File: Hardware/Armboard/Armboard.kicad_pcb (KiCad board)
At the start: 2 copper layers, 124.8 x 100.4 mm, 111 parts, among them J1 Test_Point, SW1 SW_Push, SW2 SW_Push, SW3 SW_Push, SW4 SW_Push, SW5 SW_Push, SW6 SW_Push, U1 LM2576D2TR4, U2 TM4C129E_Launchpad

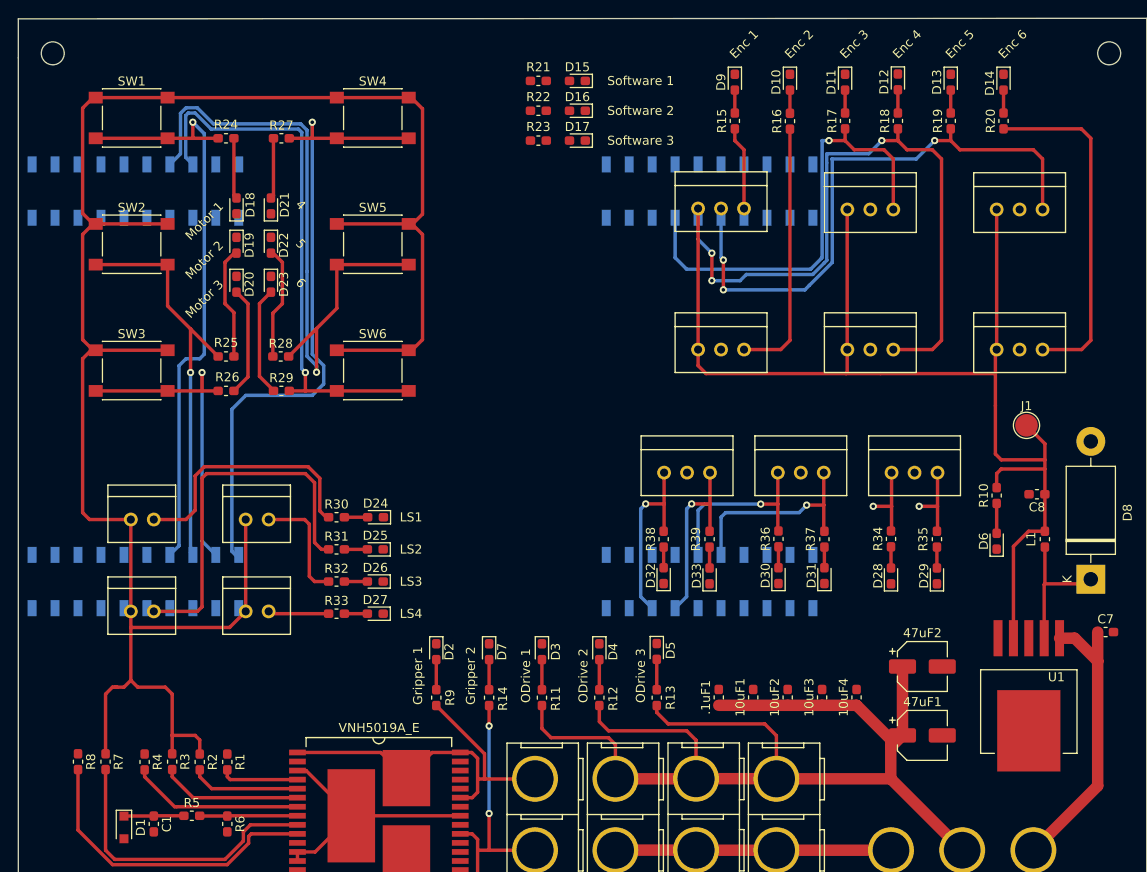
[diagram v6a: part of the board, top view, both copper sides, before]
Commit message: Added more tiva connections. Moved LS connectors away from tiva pins. Started moving ENC connectors away from tiva pins.
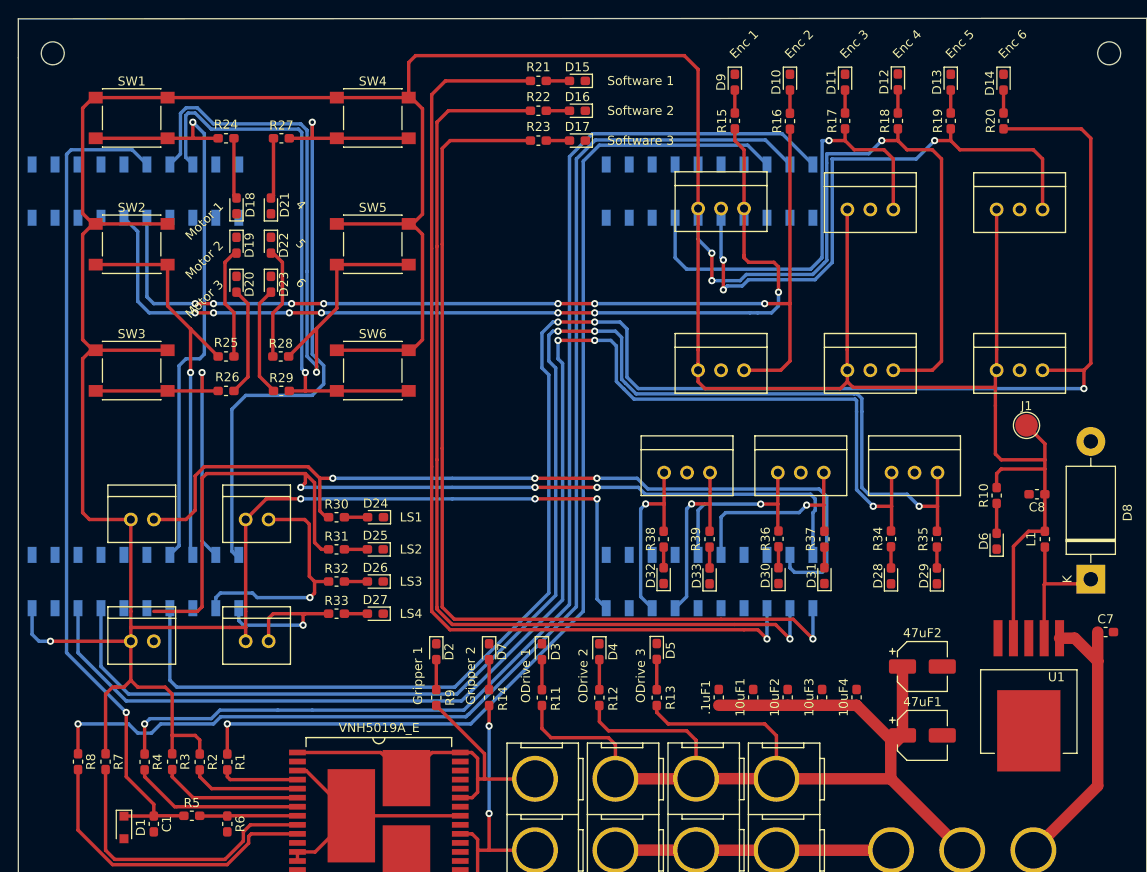
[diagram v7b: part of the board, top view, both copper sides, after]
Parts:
- moved Conn15 3.30 mm to (87.4, 107.7)
- moved Conn17 3.30 mm to (100.1, 107.7)
- moved Conn11 2.29 mm to (166.6, 77.7)
- moved Conn13 2.29 mm to (183.1, 77.7)
- moved Conn9 2.29 mm to (150.1, 77.7)
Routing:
- net Enc_6_PWM: track 38.2 -> 192.9 mm, vias 0 -> 3
- net Tx_1_Tiva: track 8.54 -> 157.8 mm, vias 1 -> 3
- net Rx_1_Tiva: track 8.51 -> 153.3 mm, vias 1 -> 3
- net IN_B: track 0.00 -> 139.8 mm, vias 0 -> 1
- net M_PWM: track 0.00 -> 134.7 mm, vias 0 -> 1
- net +3V3: track 356.8 -> 481.5 mm, vias 0 -> 4
- net IN_A: track 0.00 -> 119.6 mm, vias 0 -> 1
- net Software_1: track 0.00 -> 110.5 mm, vias 0 -> 1
- net Software_2: track 0.00 -> 108.5 mm, vias 0 -> 1
- net Software_3: track 0.00 -> 106.7 mm, vias 0 -> 1
- net Enc_1_PWM: track 9.23 -> 104.8 mm, vias 0 -> 7
- net I_SENSE: track 6.65 -> 93.6 mm, vias 0 -> 1
- net Enc_2_PWM: track 28.9 -> 111.3 mm, vias 0 -> 7
- net LS_1: track 28.4 -> 99.1 mm, vias 0 -> 3
- net LS_2: track 41.3 -> 107.1 mm, vias 0 -> 3
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
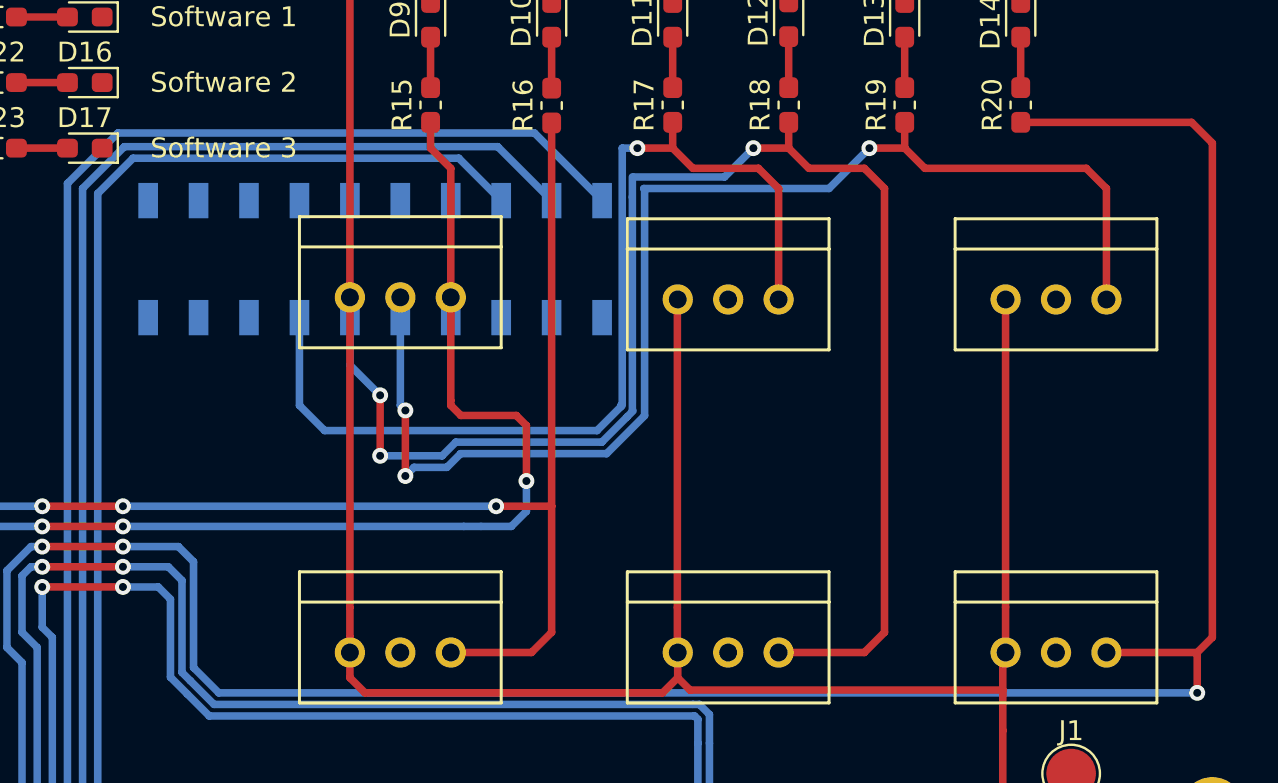
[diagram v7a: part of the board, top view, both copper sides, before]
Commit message: Finished tiva connections
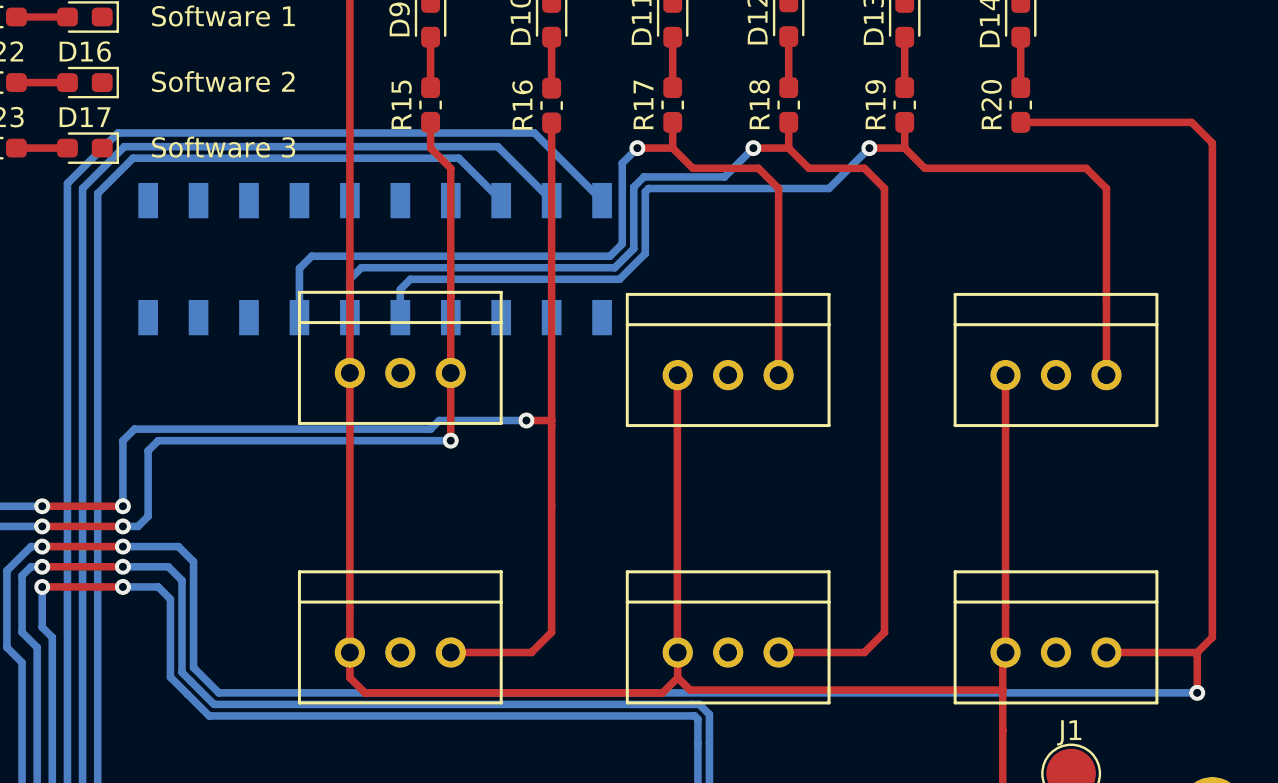
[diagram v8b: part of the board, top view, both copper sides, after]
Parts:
- moved Conn8 3.81 mm to (150.1, 63.6)
- moved Conn10 3.81 mm to (166.6, 63.8)
- moved Conn12 3.81 mm to (183.1, 63.8)
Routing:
- net Enc_4_PWM: track 76.4 -> 63.7 mm, vias 3 -> 1
- net Enc_5_PWM: track 64.6 -> 53.3 mm, vias 3 -> 1
- net +3V3: track 481.5 -> 473.9 mm
- net Enc_3_PWM: track 50.3 -> 43.0 mm
- net Enc_1_PWM: track 104.8 -> 97.8 mm
- net Enc_2_PWM: track 111.3 -> 115.1 mm
